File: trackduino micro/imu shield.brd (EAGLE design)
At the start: 43.7 x 19.6 mm, 11 parts, among them U1 LSM9DS1

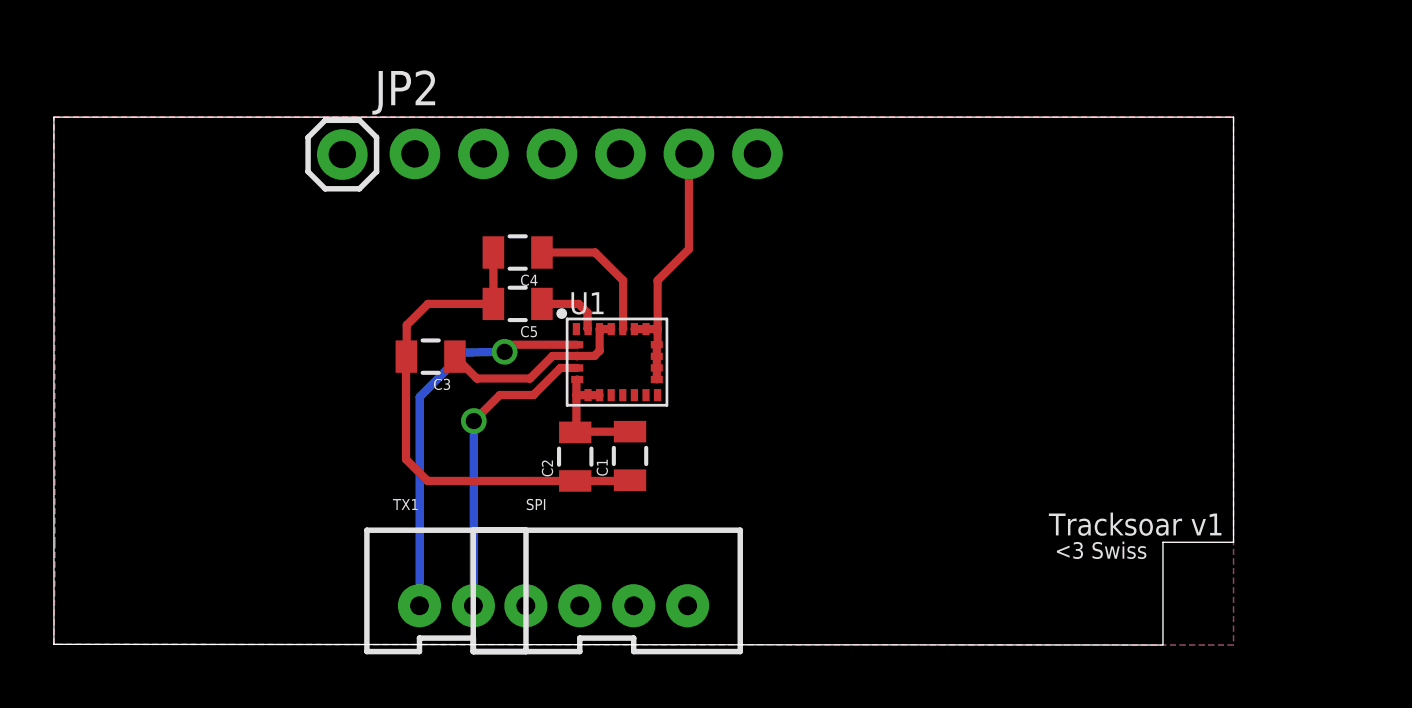
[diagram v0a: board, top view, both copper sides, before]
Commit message: added reg to imu shield
added 3v regulator to IMU shield
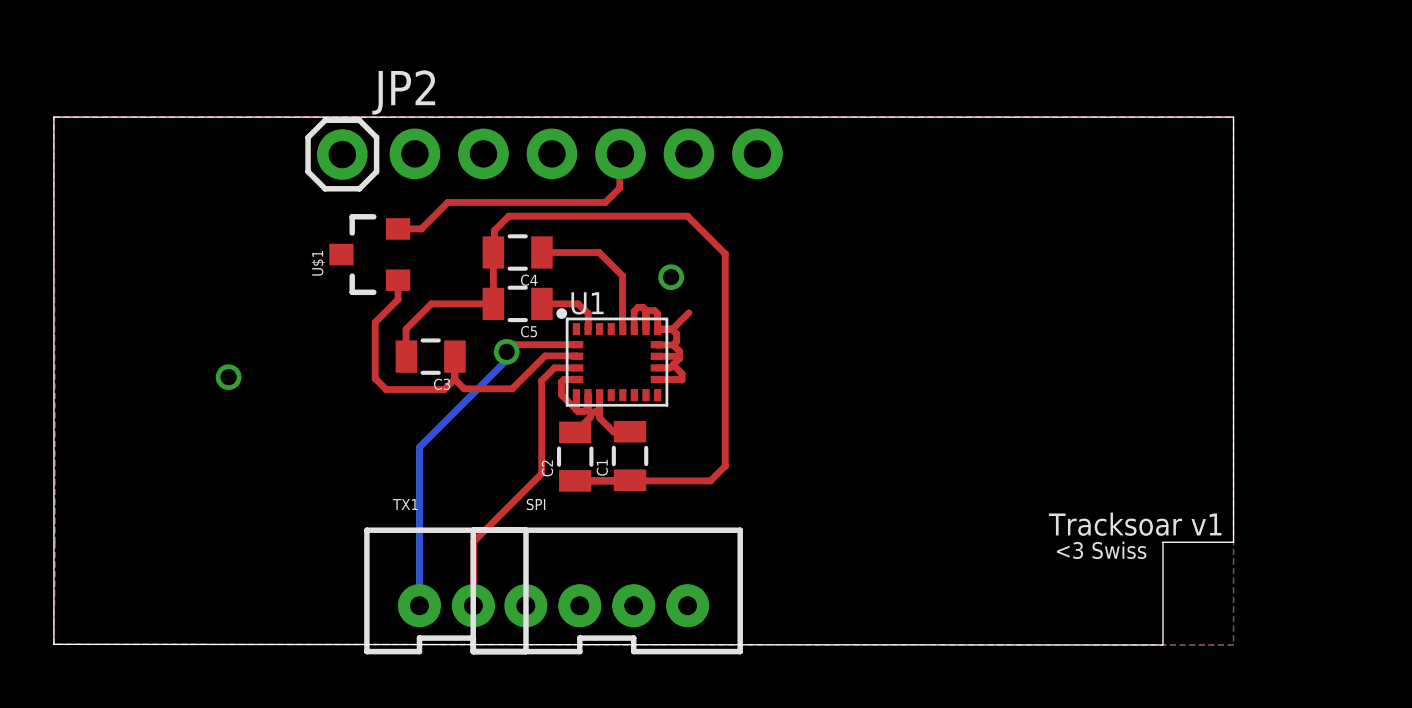
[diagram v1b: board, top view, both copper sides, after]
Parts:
- added U$1: LM3480IM4, SparkFun-PowerIC:SOT23-3
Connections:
- net GND: now also U$1.3
- net VCC: now also U$1.2
- net VDD: now also U$1.1
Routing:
- net N$1: track 19.1 -> 32.4 mm
- net VCC: track 0.00 -> 10.1 mm
- net VDD: track 7.38 -> 14.2 mm
- net 3V: track 4.89 -> 7.66 mm
- net GND: track 9.72 -> 11.0 mm, vias 0 -> 2
- net SCL: track 14.4 -> 13.5 mm
- net SDA: track 11.5 -> 10.9 mm, vias 1 -> 0

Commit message: Shield Updates
added sd storage shield, added fetid chip to programming shield. Moved
test boards to correct folder.
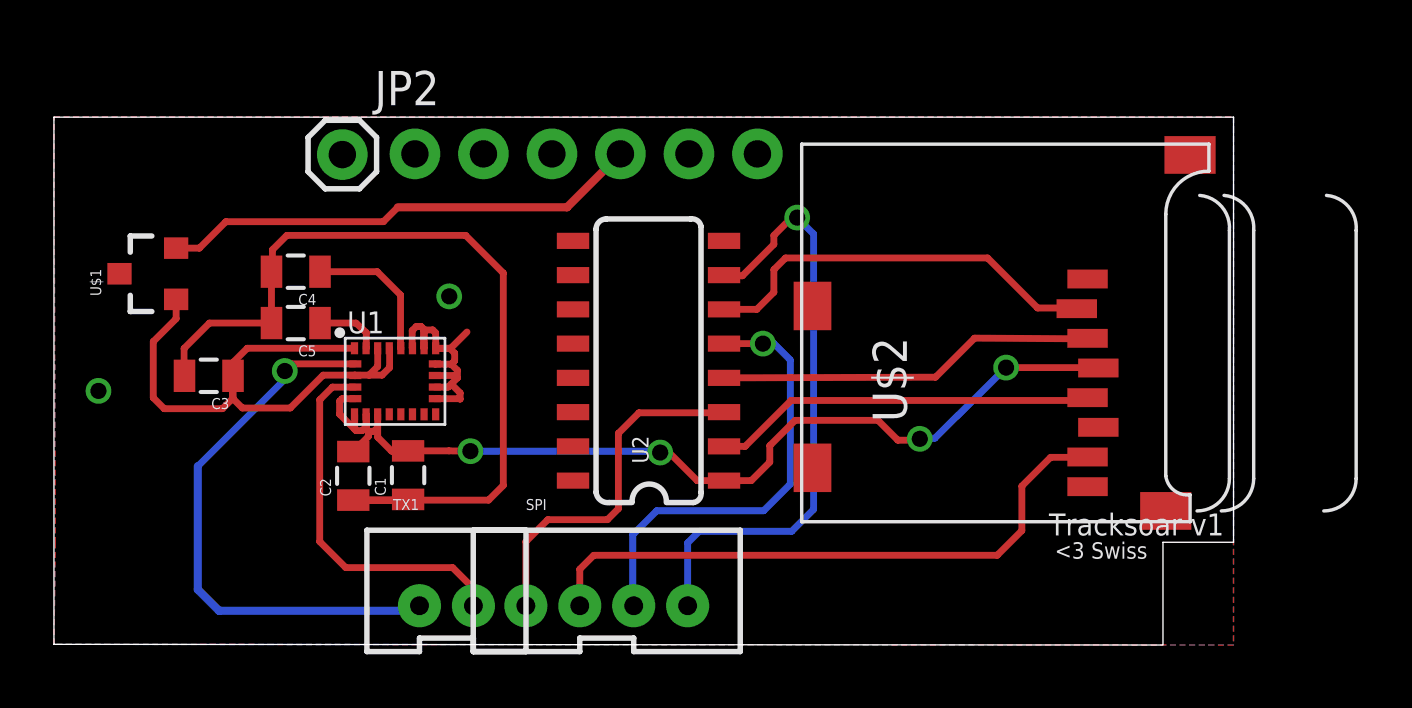
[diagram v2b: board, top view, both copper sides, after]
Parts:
- added U$2: MICROSD, adafruit:MICROSD
- added U2: HEX_CONVERTER, SparkFun-DigitalIC:SO016
- moved C4 8.26 mm to (8.56, 13.5)
- moved C5 8.26 mm to (8.56, 11.6)
- moved C3 8.26 mm to (5.33, 9.63)
- moved U$1 8.26 mm to (3.12, 13.4)
- moved U1 8.26 mm to (12.2, 9.42)
- moved C1 8.26 mm to (12.7, 5.94)
- moved C2 8.26 mm to (10.7, 5.92)
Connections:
- new net CS: U$2.2, U2.6
- new net DI: U$2.3, U2.4
- new net SCLK: U$2.5, U2.2
- net 3V: now also U$2.4, U2.1
- net GND: now also U$2.6, U$2.MT1, U$2.MT2, U2.11, U2.14, U2.8, U2.9
- net MISO: now also U$2.7
- net MOSI: now also U2.5
- net SCK: now also U2.3
- net SS: now also U2.7
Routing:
- net 3V: track 7.66 -> 36.4 mm, vias 0 -> 4
- net MISO: track 0.00 -> 22.9 mm
- net SS: track 0.00 -> 22.4 mm, vias 0 -> 1
- net MOSI: track 0.00 -> 16.6 mm, vias 0 -> 1
- net CS: track 0.00 -> 15.1 mm
- net SCLK: track 0.00 -> 14.2 mm
- net DI: track 0.00 -> 14.1 mm
- net SCK: track 0.00 -> 13.4 mm
- net VDD: track 14.2 -> 22.6 mm
- net VCC: track 10.1 -> 18.0 mm
- net SCL: track 13.5 -> 20.8 mm
- net SDA: track 10.9 -> 13.9 mm
